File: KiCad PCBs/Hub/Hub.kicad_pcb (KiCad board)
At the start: 2 copper layers, 1 part, among them J1 Conn_02x04_Top_Bottom

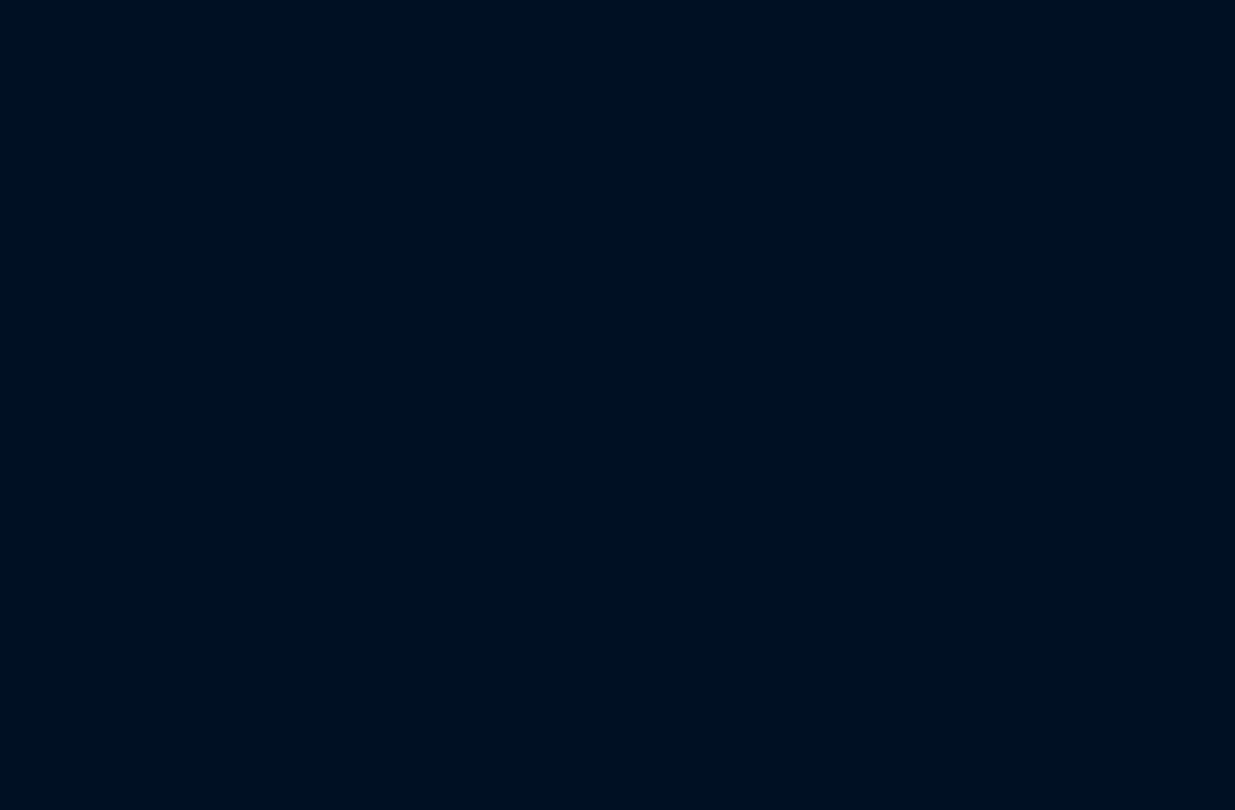
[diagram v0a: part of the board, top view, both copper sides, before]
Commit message: Added power status LEDs to Master PCB
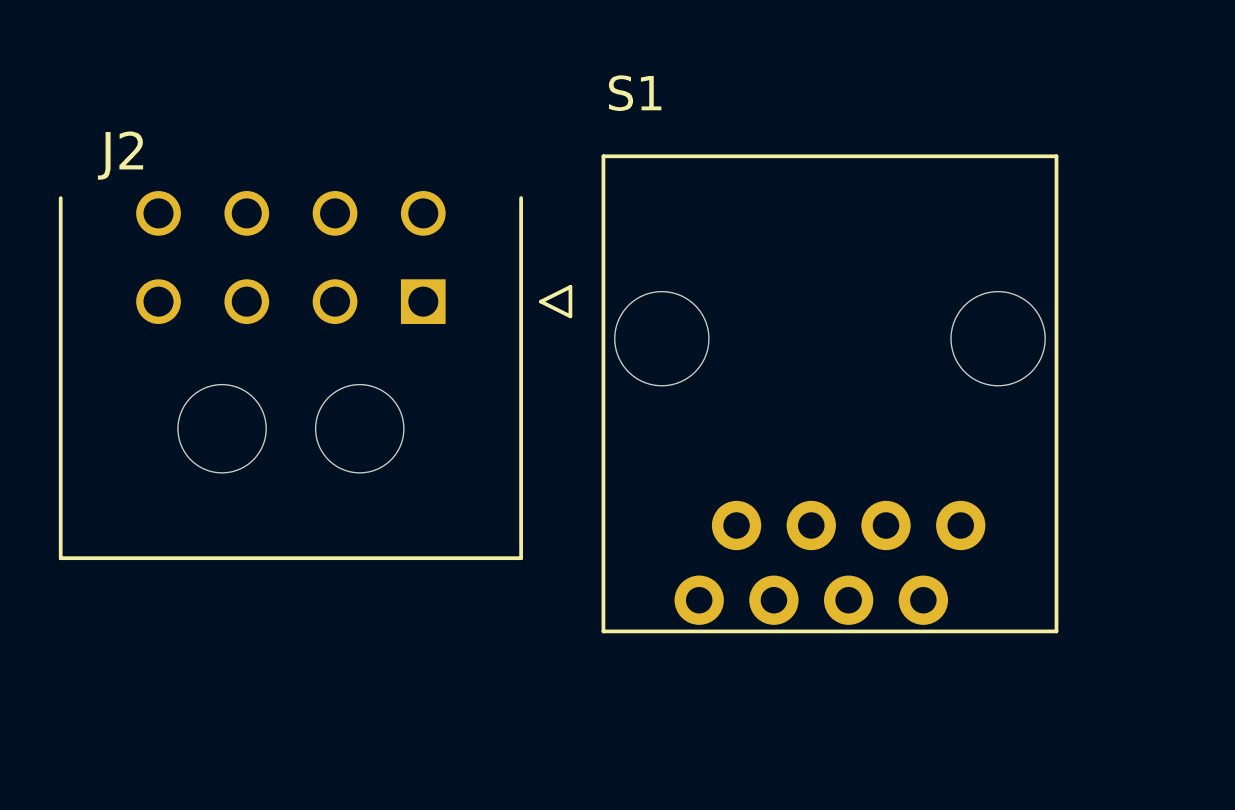
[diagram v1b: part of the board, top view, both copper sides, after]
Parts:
- added J2: Conn_02x04_Top_Bottom, A10 KiCad Libraries:Molex 43045-0800, F.Cu at (135.9, 90.2)
- added S1: 8P8C, A10 KiCad Libraries:RJ45-8P8C, F.Cu at (149.7, 91.4)
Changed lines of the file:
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@@
   (net 5 "RS485-B")
   (net 6 "RS485-A")
+  (net 7 "unconnected-(J2-Pad3)")
+  (net 8 "unconnected-(J2-Pad4)")
+  (net 9 "unconnected-(S1-Pad1)")
+  (net 10 "unconnected-(S1-Pad2)")
+  (net 11 "unconnected-(S1-Pad3)")
+  (net 12 "unconnected-(S1-Pad4)")
+  (net 13 "unconnected-(S1-Pad5)")
+  (net 14 "unconnected-(S1-Pad6)")
+  (net 15 "unconnected-(S1-Pad7)")
+  (net 16 "unconnected-(S1-Pad8)")
+  (footprint "A10 KiCad Libraries:Molex 43045-0800" (layer "F.Cu")
+    (at 135.89 90.17)
+    (descr "43045-08(00,01,02,10)")
+    (tags "Connector")
+    (property "Field4" "Daisy-Chain")
+    (property "Sheetfile" "Hub.kicad_sch")
+    (property "Sheetname" "")
+    (attr through_hole)
+    (fp_text reference "J2" (at -10.16 -5.08) (layer "F.SilkS")
+      (effects (font (size 1.27 1.27) (thickness 0.254)))
+    )
+    (fp_text value "Conn_02x04_Top_Bottom" (at 0 0) (layer "F.SilkS") hide
+      (effects (font (size 1.27 1.27) (thickness 0.254)))
+    )
+    (fp_text user "${REFERENCE}" (at 0 0) (layer "F.Fab")
+      (effects (font (size 1.27 1.27) (thickness 0.254)))
+    )
+    (fp_line (start 3.325 8.72) (end -12.325 8.72) (layer "F.SilkS") (width 0.127))
+    (fp_line (start 3.325 -3.52) (end 3.325 8.72) (layer "F.SilkS") (width 0.127))
+    (fp_line (start 4 0) (end 5 -0.5) (layer "F.SilkS") (width 0.127))
+    (fp_line (start 5 -0.5) (end 5 0.5) (layer "F.SilkS") (width 0.127))
+    (fp_line (start -12.325 8.72) (end -12.325 -3.52) (layer "F.SilkS") (width 0.127))
+    (fp_line (start 5 0.5) (end 4 0) (layer "F.SilkS") (width 0.127))
+    (fp_line (start 4.595 -4.9792) (end 4.595 9.99) (layer "F.CrtYd") (width 0.05))
+    (fp_line (start -13.595 -4.9792) (end 4.595 -4.9792) (layer "F.CrtYd") (width 0.05))
+    (fp_line (start 4.595 9.99) (end -13.595 9.99) (layer "F.CrtYd") (width 0.05))
+    (fp_line (start -13.595 9.99) (end -13.595 -4.9792) (layer "F.CrtYd") (width 0.05))
+    (fp_line (start 4 0) (end 5 -0.5) (layer "F.Fab") (width 0.127))
+    (fp_line (start -12.325 8.72) (end -12.325 -3.52) (layer "F.Fab") (width 0.127))
+    (fp_line (start 3.325 -3.52) (end 3.325 8.72) (layer "F.Fab") (width 0.127))
+    (fp_line (start 3.325 8.72) (end -12.325 8.72) (layer "F.Fab") (width 0.127))
+    (fp_line (start -12.325 -3.52) (end 3.325 -3.52) (layer "F.Fab") (width 0.127))
+    (fp_line (start 5 0.5) (end 4 0) (layer "F.Fab") (width 0.127))
+    (fp_line (start 5 -0.5) (end 5 0.5) (layer "F.Fab") (width 0.127))
+    (pad "" np_thru_hole circle (at -2.16 4.32) (size 3 3) (drill 3) (layers *.Cu *.Mask))
+    (pad "" np_thru_hole circle (at -6.84 4.32) (size 3 3) (drill 3) (layers *.Cu *.Mask))
+    (pad "1" thru_hole rect (at 0 0) (size 1.52 1.52) (drill 1.02) (layers *.Cu *.Mask)
+      (net 1 "12V") (pinfunction "Pin_1") (pintype "passive"))
+    (pad "2" thru_hole circle (at -3 0) (size 1.52 1.52) (drill 1.02) (layers *.Cu *.Mask)
+      (net 2 "GND") (pinfunction "Pin_2") (pintype "passive"))
+    (pad "3" thru_hole circle (at -6 0) (size 1.52 1.52) (drill 1.02) (layers *.Cu *.Mask)
+      (net 7 "unconnected-(J2-Pad3)") (pinfunction "Pin_3") (pintype "passive+no_connect"))
+    (pad "4" thru_hole circle (at -9 0) (size 1.52 1.52) (drill 1.02) (layers *.Cu *.Mask)
+      (net 8 "unconnected-(J2-Pad4)") (pinfunction "Pin_4") (pintype "passive+no_connect"))
+    (pad "5" thru_hole circle (at 0 -3) (size 1.52 1.52) (drill 1.02) (layers *.Cu *.Mask)
+      (net 1 "12V") (pinfunction "Pin_5") (pintype "passive"))
+    (pad "6" thru_hole circle (at -3 -3) (size 1.52 1.52) (drill 1.02) (layers *.Cu *.Mask)
+      (net 2 "GND") (pinfunction "Pin_6") (pintype "passive"))
+    (pad "7" thru_hole circle (at -6 -3) (size 1.52 1.52) (drill 1.02) (layers *.Cu *.Mask)
+      (net 5 "RS485-B") (pinfunction "Pin_7") (pintype "passive"))
+    (pad "8" thru_hole circle (at -9 -3) (size 1.52 1.52) (drill 1.02) (layers *.Cu *.Mask)
+      (net 6 "RS485-A") (pinfunction "Pin_8") (pintype "passive"))
+    (model "${KIPRJMOD}/../../KiCad Libraries/43045-0800.stp"
+      (offset (xyz -4.445 -3.937 3.81))
+      (scale (xyz 1 1 1))
+      (rotate (xyz -90 0 0))
+    )
+  )
   (footprint "A10 KiCad Libraries:Molex 43045-0800" (layer "F.Cu")
     (at 208.915 92.075 90)
     (descr "43045-08(00,01,02,10)")
     (tags "Connector")
+    (property "Field4" "Uplink")
     (property "Sheetfile" "Hub.kicad_sch")
     (property "Sheetname" "")
@@
     )
   )
+  (footprint "A10 KiCad Libraries:RJ45-8P8C" (layer "F.Cu")
+    (at 149.7135 91.4293)
+    (property "Sheetfile" "Hub.kicad_sch")
+    (property "Sheetname" "")
+    (fp_text reference "S1" (at -7.62 -7.62) (layer "F.SilkS")
+      (effects (font (size 1.1684 1.1684) (thickness 0.1016)) (justify left bottom))
+    )
+    (fp_text value "8P8C" (at -6.35 -3.81) (layer "F.Fab")
+      (effects (font (size 1.1684 1.1684) (thickness 0.1016)) (justify left bottom))
+    )
+    (fp_line (start 7.7 -6.2) (end 7.7 9.95) (layer "F.SilkS") (width 0.127))
+    (fp_line (start -7.7 -6.2) (end 7.7 -6.2) (layer "F.SilkS") (width 0.127))
+    (fp_line (start -7.7 9.95) (end -7.7 -6.2) (layer "F.SilkS") (width 0.127))
+    (fp_line (start 7.7 9.95) (end -7.7 9.95) (layer "F.SilkS") (width 0.127))
+    (pad "" np_thru_hole circle (at 5.715 0) (size 3.2 3.2) (drill 3.2) (layers *.Cu *.Mask))
+    (pad "" np_thru_hole circle (at -5.715 0) (size 3.2 3.2) (drill 3.2) (layers *.Cu *.Mask))
+    (pad "1" thru_hole circle (at 4.445 6.35) (size 1.6764 1.6764) (drill 0.9) (layers *.Cu *.Mask)
+      (net 9 "unconnected-(S1-Pad1)") (pintype "passive") (solder_mask_margin 0.1016))
+    (pad "2" thru_hole circle (at 3.175 8.89) (size 1.6764 1.6764) (drill 0.9) (layers *.Cu *.Mask)
+      (net 10 "unconnected-(S1-Pad2)") (pintype "passive") (solder_mask_margin 0.1016))
+    (pad "3" thru_hole circle (at 1.905 6.35) (size 1.6764 1.6764) (drill 0.9) (layers *.Cu *.Mask)
+      (net 11 "unconnected-(S1-Pad3)") (pintype "passive") (solder_mask_margin 0.1016))
+    (pad "4" thru_hole circle (at 0.635 8.89) (size 1.6764 1.6764) (drill 0.9) (layers *.Cu *.Mask)
+      (net 12 "unconnected-(S1-Pad4)") (pintype "passive") (solder_mask_margin 0.1016))
+    (pad "5" thru_hole circle (at -0.635 6.35) (size 1.6764 1.6764) (drill 0.9) (layers *.Cu *.Mask)
+      (net 13 "unconnected-(S1-Pad5)") (pintype "passive") (solder_mask_margin 0.1016))
+    (pad "6" thru_hole circle (at -1.905 8.89) (size 1.6764 1.6764) (drill 0.9) (layers *.Cu *.Mask)
+      (net 14 "unconnected-(S1-Pad6)") (pintype "passive") (solder_mask_margin 0.1016))
+    (pad "7" thru_hole circle (at -3.175 6.35) (size 1.6764 1.6764) (drill 0.9) (layers *.Cu *.Mask)
+      (net 15 "unconnected-(S1-Pad7)") (pintype "passive") (solder_mask_margin 0.1016))
+    (pad "8" thru_hole circle (at -4.445 8.89) (size 1.6764 1.6764) (drill 0.9) (layers *.Cu *.Mask)
+      (net 16 "unconnected-(S1-Pad8)") (pintype "passive") (solder_mask_margin 0.1016))
+    (model "${KICAD6_3DMODEL_DIR}/Connector_RJ.3dshapes/RJ45_Amphenol_RJHSE538X.step"
+      (offset (xyz -3.429 -1.905 0))
+      (scale (xyz 1 1 1))
+      (rotate (xyz 0 0 0))
+    )
+  )

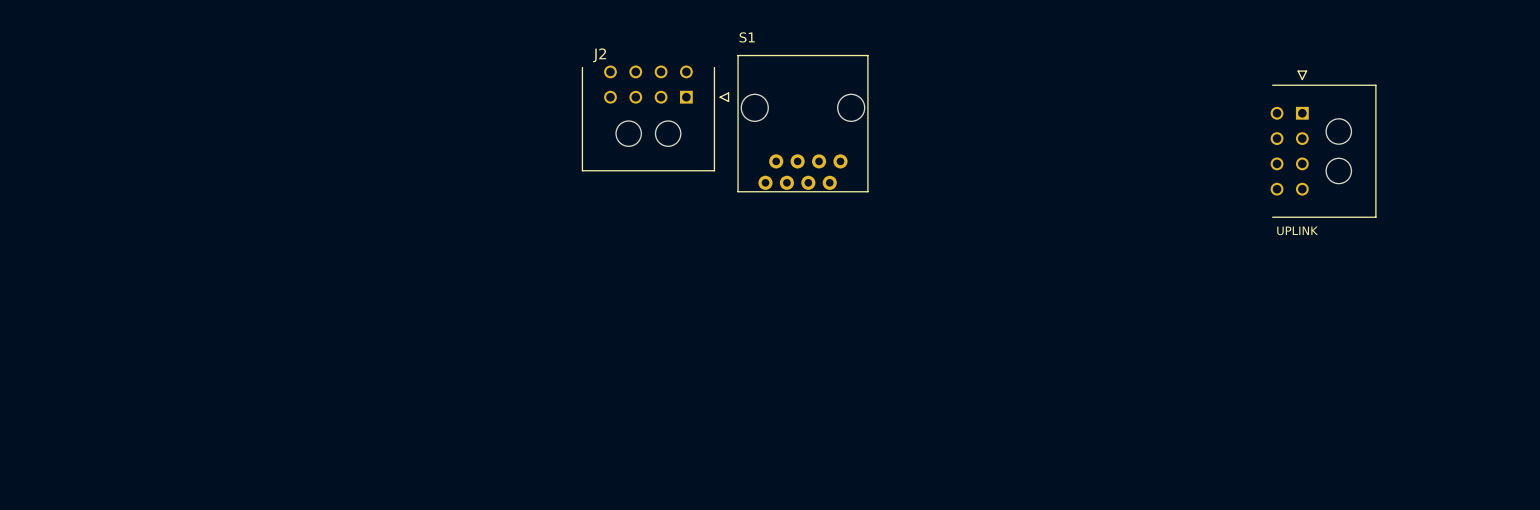
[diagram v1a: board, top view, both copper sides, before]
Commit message: Updated Master PCB and completed first version of Hub
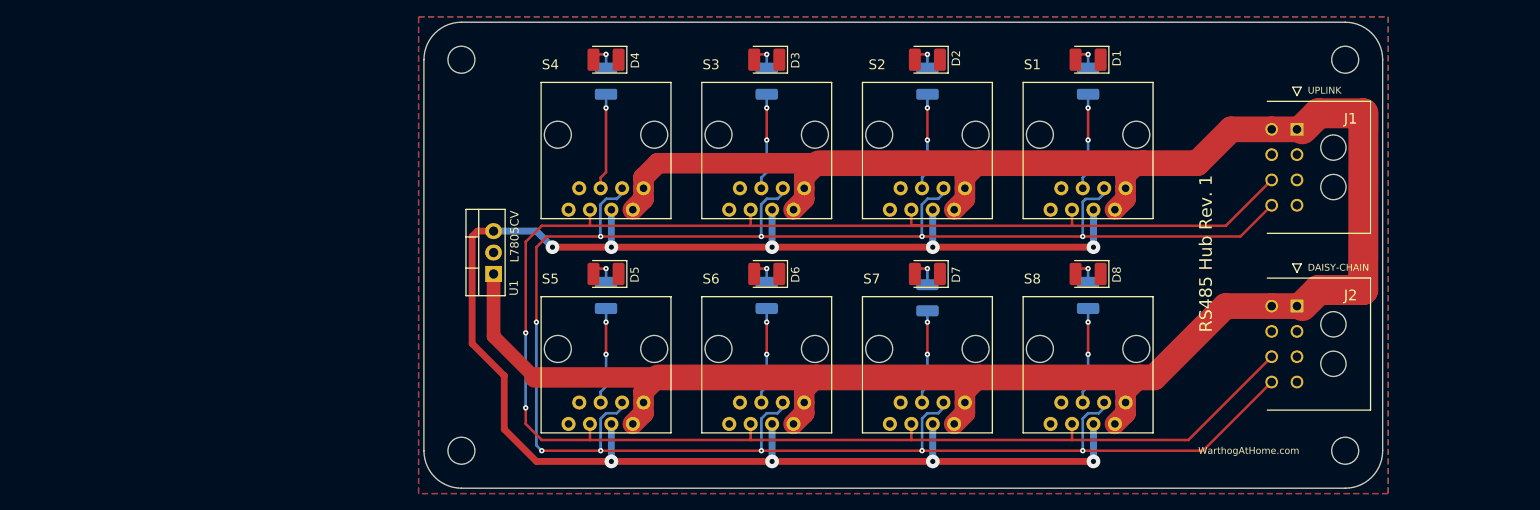
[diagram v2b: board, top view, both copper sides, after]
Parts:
- added D1: LED, LED_SMD:LED_1210_3225Metric_Pad1.42x2.65mm_HandSolder, F.Cu at (183.5, 85.7)
- added D2: LED, LED_SMD:LED_1210_3225Metric_Pad1.42x2.65mm_HandSolder, F.Cu at (164.5, 85.7)
- added D3: LED, LED_SMD:LED_1210_3225Metric_Pad1.42x2.65mm_HandSolder, F.Cu at (145.4, 85.7)
- added D4: LED, LED_SMD:LED_1210_3225Metric_Pad1.42x2.65mm_HandSolder, F.Cu at (126.4, 85.7)
- added D5: LED, LED_SMD:LED_1210_3225Metric_Pad1.42x2.65mm_HandSolder, F.Cu at (126.4, 111.1)
- added D6: LED, LED_SMD:LED_1210_3225Metric_Pad1.42x2.65mm_HandSolder, F.Cu at (145.4, 111.1)
- added D7: LED, LED_SMD:LED_1210_3225Metric_Pad1.42x2.65mm_HandSolder, F.Cu at (164.5, 111.1)
- added D8: LED, LED_SMD:LED_1210_3225Metric_Pad1.42x2.65mm_HandSolder, F.Cu at (183.5, 111.1)
- added HOLE-1: MountingHole_3.2mm_M3, MountingHole:MountingHole_3.2mm_M3, F.Cu at (109.2, 85.7)
- added HOLE-2: MountingHole_3.2mm_M3, MountingHole:MountingHole_3.2mm_M3, F.Cu at (214.0, 85.7)
- added HOLE-3: MountingHole_3.2mm_M3, MountingHole:MountingHole_3.2mm_M3, F.Cu at (109.2, 132.1)
- added HOLE-4: MountingHole_3.2mm_M3, MountingHole:MountingHole_3.2mm_M3, F.Cu at (214.0, 132.1)
- added R1: 400R, Resistor_SMD:R_1210_3225Metric_Pad1.30x2.65mm_HandSolder, B.Cu at (183.5, 88.3)
- added R2: 400R, Resistor_SMD:R_1210_3225Metric_Pad1.30x2.65mm_HandSolder, B.Cu at (164.5, 88.3)
- added R3: 400R, Resistor_SMD:R_1210_3225Metric_Pad1.30x2.65mm_HandSolder, B.Cu at (145.4, 88.3)
- added R4: 400R, Resistor_SMD:R_1210_3225Metric_Pad1.30x2.65mm_HandSolder, B.Cu at (126.4, 88.3)
- added R5: 400R, Resistor_SMD:R_1210_3225Metric_Pad1.30x2.65mm_HandSolder, B.Cu at (126.4, 113.7)
- added R6: 400R, Resistor_SMD:R_1210_3225Metric_Pad1.30x2.65mm_HandSolder, B.Cu at (145.4, 113.7)
- added R7: 400R, Resistor_SMD:R_1210_3225Metric_Pad1.30x2.65mm_HandSolder, B.Cu at (164.5, 113.9)
- added R8: 400R, Resistor_SMD:R_1210_3225Metric_Pad1.30x2.65mm_HandSolder, B.Cu at (183.5, 113.7)
- added S2: 8P8C, A10 KiCad Libraries:RJ45-8P8C, F.Cu at (164.5, 94.6)
- added S3: 8P8C, A10 KiCad Libraries:RJ45-8P8C, F.Cu at (145.4, 94.6)
- added S4: 8P8C, A10 KiCad Libraries:RJ45-8P8C, F.Cu at (126.4, 94.6)
- added S5: 8P8C, A10 KiCad Libraries:RJ45-8P8C, F.Cu at (126.4, 120.0)
- added S6: 8P8C, A10 KiCad Libraries:RJ45-8P8C, F.Cu at (145.4, 120.0)
- added S7: 8P8C, A10 KiCad Libraries:RJ45-8P8C, F.Cu at (164.5, 120.0)
- added S8: 8P8C, A10 KiCad Libraries:RJ45-8P8C, F.Cu at (183.5, 120.0)
- added U1: L7805CV, Package_TO_SOT_THT:TO-220-3_Vertical, F.Cu at (113.0, 111.1)
- moved J2 76.5 mm to (208.3, 114.9), turned to 90 degrees
- moved S1 34.0 mm to (183.5, 94.6)
- moved J1 2.01 mm to (208.3, 94.0)
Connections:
- S1 pad 1: unconnected-(S1-Pad1) -> 12V
- S1 pad 2: unconnected-(S1-Pad2) -> 12V
- S1 pad 3: unconnected-(S1-Pad3) -> RS485-A
- S1 pad 4: unconnected-(S1-Pad4) -> 5V
- S1 pad 5: unconnected-(S1-Pad5) -> 5V_S1
- S1 pad 6: unconnected-(S1-Pad6) -> RS485-B
- S1 pad 7: unconnected-(S1-Pad7) -> GND
- S1 pad 8: unconnected-(S1-Pad8) -> GND
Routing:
- net 12V: track 0.00 -> 278.2 mm
- net RS485-A: track 0.00 -> 263.9 mm, vias 0 -> 10
- net RS485-B: track 0.00 -> 222.9 mm, vias 0 -> 2
- net 5V: track 0.00 -> 206.1 mm, vias 0 -> 9
- net 5V_S4: track 0.00 -> 11.4 mm, vias 0 -> 1
- net 5V_S3: track 0.00 -> 11.4 mm, vias 0 -> 2
- net 5V_S2: track 0.00 -> 11.4 mm, vias 0 -> 2
- net 5V_S1: track 0.00 -> 11.4 mm, vias 0 -> 2
- net 5V_S8: track 0.00 -> 11.4 mm, vias 0 -> 2
- net 5V_S6: track 0.00 -> 11.4 mm, vias 0 -> 2
- net 5V_S5: track 0.00 -> 11.4 mm, vias 0 -> 2
- net 5V_S7: track 0.00 -> 11.1 mm, vias 0 -> 2
- net Net-(D7-Pad2): track 0.00 -> 3.66 mm, vias 0 -> 1
- net Net-(D5-Pad2): track 0.00 -> 3.38 mm, vias 0 -> 1
- net Net-(D2-Pad2): track 0.00 -> 3.38 mm, vias 0 -> 1
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- added copper zone on B.Cu, net GND
- added copper zone on F.Cu, net GND
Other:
- board outline added: 113.7 x 55.2 mm
- board text added: "BRRRRRRRRRRT"
- board text added: "RS485 Hub Rev. 1"
- board text added: "WarthogAtHome.com"

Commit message: First version of Hub completed
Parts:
- removed D1, D2, D3, D4, D5, D6, D7, D8: LED, LED_SMD:LED_1210_3225Metric_Pad1.42x2.65mm_HandSolder
- removed HOLE-1: MountingHole_3.2mm_M3, MountingHole:MountingHole_3.2mm_M3
- removed S1, S2, S3, S4, S5, S6, S7, S8: 8P8C, A10 KiCad Libraries:RJ45-8P8C
- removed U1: L7805CV, Package_TO_SOT_THT:TO-220-3_Vertical
- added R10: 1.8K, A10 KiCad Libraries:R0805, F.Cu at (112.6, 91.7)
- added R11: 390R, A10 KiCad Libraries:R0805, F.Cu at (197.1, 91.7)
- added R12: 1.8K, A10 KiCad Libraries:R0805, F.Cu at (187.5, 91.7)
- added R13: 390R, A10 KiCad Libraries:R0805, F.Cu at (137.9, 91.7)
- added R14: 1.8K, A10 KiCad Libraries:R0805, F.Cu at (128.4, 91.7)
- added R15: 390R, A10 KiCad Libraries:R0805, F.Cu at (214.7, 91.7)
- added R16: 1.8K, A10 KiCad Libraries:R0805, F.Cu at (203.3, 91.7)
- added R9: 390R, A10 KiCad Libraries:R0805, F.Cu at (122.1, 91.7)
- added U2: RJ45-B-1*4, A10 KiCad Libraries:RJ45-TH_B-1-4, F.Cu at (108.4, 103.7)
- added U3: RJ45-B-1*4, A10 KiCad Libraries:RJ45-TH_B-1-4, F.Cu at (183.4, 103.7)
- J1, J2: footprint A10 KiCad Libraries:Molex 43045-0800 -> A10 KiCad Libraries:Molex Micro-Fit 3.0 43045-0800
- R1, R3, R5, R7: value 400R -> 390R; footprint Resistor_SMD:R_1210_3225Metric_Pad1.30x2.65mm_HandSolder -> A10 KiCad Libraries:R0805; moved to F.Cu
- R2, R4, R6, R8: value 400R -> 1.8K; footprint Resistor_SMD:R_1210_3225Metric_Pad1.30x2.65mm_HandSolder -> A10 KiCad Libraries:R0805; moved to F.Cu
- moved J2 144.2 mm to (65.9, 92.3), turned to -90 degrees
- moved R1 92.9 mm to (90.6, 91.7), turned to 0 degrees
- moved R2 83.4 mm to (81.1, 91.7), turned to 180 degrees
- moved HOLE-2 68.7 mm to (145.9, 94.8)
- moved R6 53.2 mm to (97.0, 91.7), turned to 180 degrees
- moved HOLE-3 52.9 mm to (62.7, 106.9)
- moved R4 29.9 mm to (156.1, 91.7), turned to 180 degrees
- moved R5 29.7 mm to (106.4, 91.7), turned to 0 degrees
- moved HOLE-4 29.4 mm to (229.1, 106.9)
- moved R7 27.9 mm to (181.3, 91.7), turned to 0 degrees
- moved R8 24.9 mm to (171.8, 91.7), turned to 180 degrees
- moved R3 20.4 mm to (165.6, 91.7), turned to 0 degrees
- moved J1 17.5 mm to (225.7, 92.5)
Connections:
- net RS485-A renamed RS485+
- net RS485-B renamed RS485-
- R1 pad 1: 5V_S1 -> GND
- R2 pad 1: 5V_S2 -> GND
- R3 pad 1: 5V_S3 -> GND
- R4 pad 1: 5V_S4 -> GND
- R5 pad 1: 5V_S5 -> GND
- R6 pad 1: 5V_S6 -> GND
- R7 pad 1: 5V_S7 -> GND
- R8 pad 1: 5V_S8 -> GND
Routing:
- net 5V: track 206.1 -> 0.00 mm, vias 9 -> 0
- net 12V: track 278.2 -> 365.6 mm
- net RS485-: track 222.9 -> 259.2 mm, vias 2 -> 0
- net RS485+: track 263.9 -> 254.5 mm, vias 10 -> 16
- net Net-(R15-Pad2): track 0.00 -> 5.36 mm
- net Net-(R16-Pad2): track 0.00 -> 5.36 mm
- net Net-(R14-Pad2): track 0.00 -> 5.36 mm
- net Net-(R12-Pad2): track 0.00 -> 5.36 mm
- net Net-(R10-Pad2): track 0.00 -> 5.36 mm
- net Net-(R9-Pad2): track 0.00 -> 5.35 mm
- net Net-(R11-Pad2): track 0.00 -> 5.35 mm
- net Net-(R13-Pad2): track 0.00 -> 5.35 mm
- net 5V_S4: track 11.4 -> 7.01 mm, vias 1 -> 0
- net 5V_S2: track 11.4 -> 7.01 mm, vias 2 -> 0
- net 5V_S1: track 11.4 -> 7.01 mm, vias 2 -> 0
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- added copper zone on F.Cu, net 12V
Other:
- board size 113.7 x 55.2 mm -> 175.3 x 29.2 mm
- rule pad_to_mask_clearance: 0.0508 -> 0
- board text added: "DCS-BIOS RS485 Hub Rev. 1"
- board text removed: "RS485 Hub Rev. 1"
